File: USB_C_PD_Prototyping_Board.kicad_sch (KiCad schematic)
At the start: 48 parts, among them IC1 TPS259474LRPWR, IC2 BD33FC0FP-E2, J1 USB_C_Receptacle, J2 Power_out, J3 Data_out, J5 Conn_01x04_Pin, J6 Conn_02x02_Counter_Clockwise, J7 Conn_02x02_Counter_Clockwise, Q1 DMP3018SFV-7, Q2 DMP3018SFV-7, SW1 Power_out_switch, U1 HUSB238_xxxDD

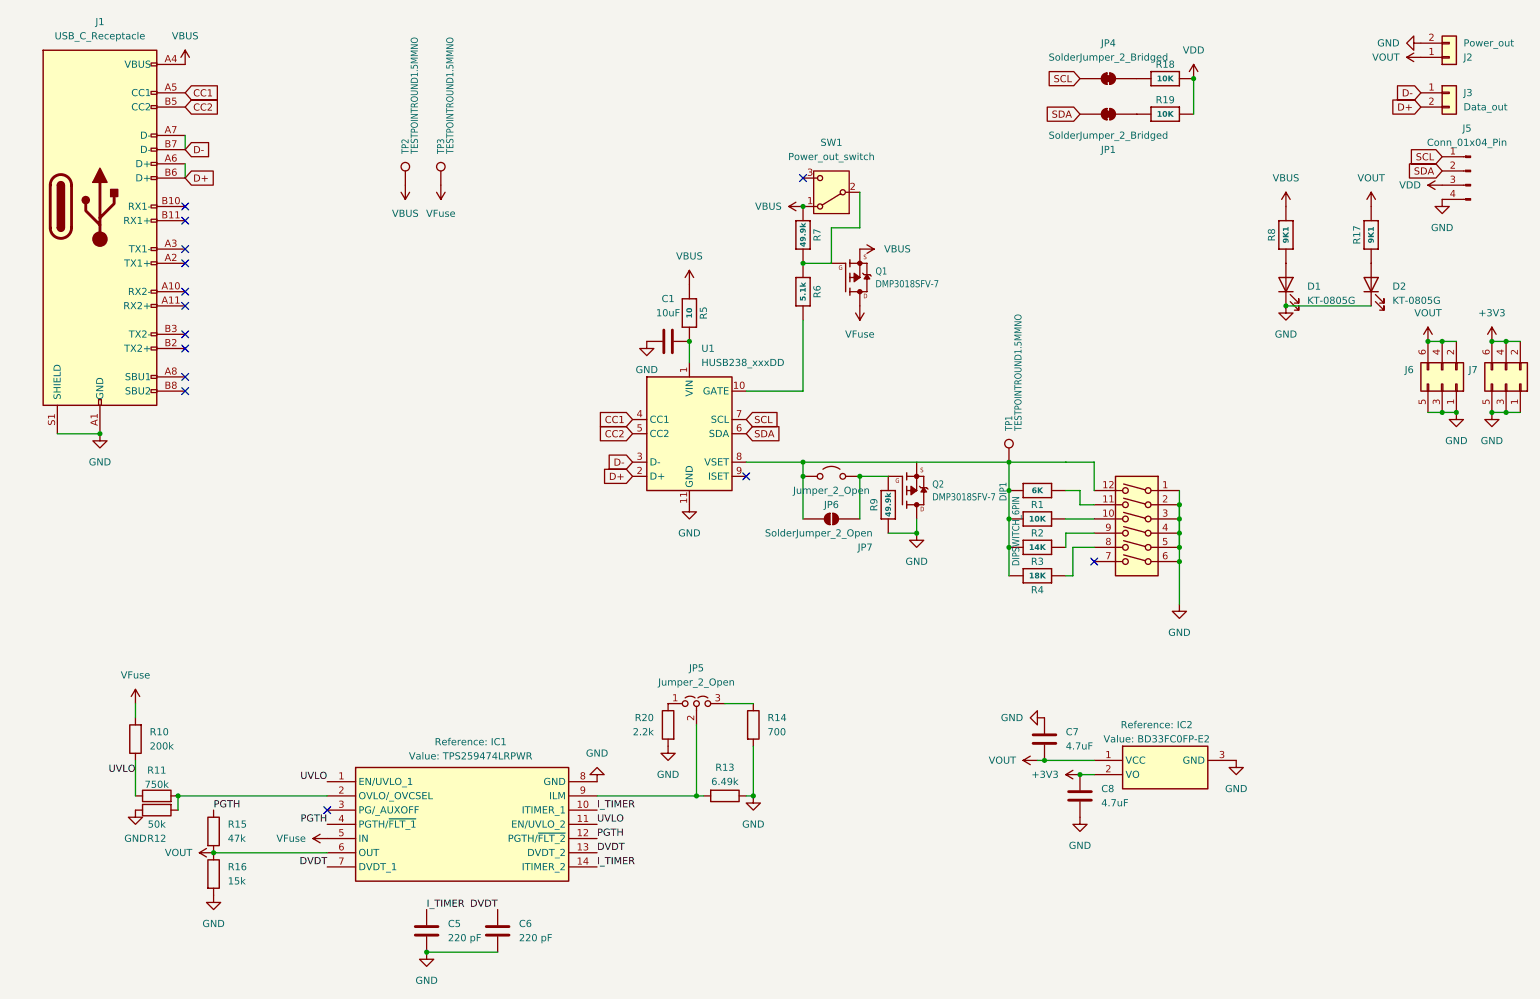
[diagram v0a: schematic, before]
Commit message: Re-worked after initial tests
- Corrected silkscreen labels for output switch
- Corrected jumper logic polarity for voltage select
- Added ISET resistor to set default current request to 3A (instead of 3.25A for open circuit) so that 9, 12V selectable with DIP switches
- Double indicator LED limiting resistor values to reduce brightness
- Changed 3V3 reg to switch mode to solve thermals
- Added cutout to limit covering of breadboard rows
- Made as many resistors as possible THT to use as a soldering task (will spin up an SMD only one as a cheaper out of the box solution too)
- Simplified and thickened primary current path (there wasn't a problem, but it will be more capable now)
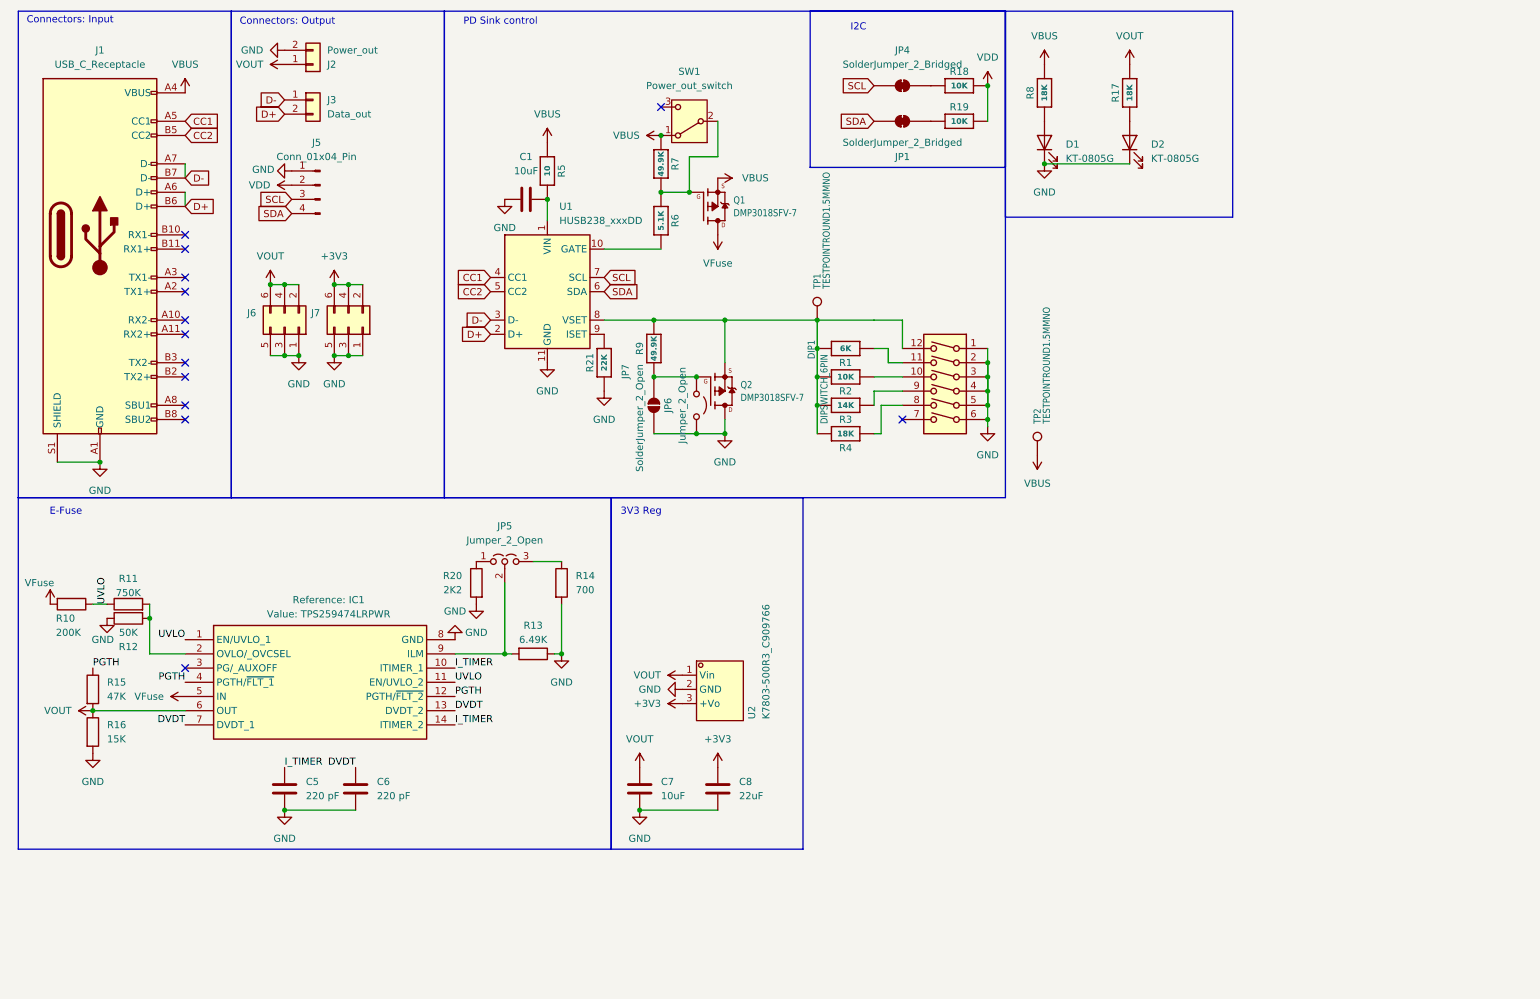
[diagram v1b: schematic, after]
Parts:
- removed IC2: BD33FC0FP-E2, Package_TO_SOT_SMD:TO-252-2, symbol Samacsys:BD33FC0FP-E2
- removed TP3: TESTPOINTROUND1.5MMNO, TestPoint:TestPoint_THTPad_2.0x2.0mm_Drill1.0mm, symbol Connector:TestPoint
- added R21: 22K, Resistor_THT:R_Axial_DIN0207_L6.3mm_D2.5mm_P7.62mm_Horizontal, symbol Adafruit USB Type C PD Switchable-eagle-import:microbuilder_RESISTOR_0402NO
- added U2: K7803-500R3_C909766, EasyEDA:PWRM-TH_K78XX-500R3, symbol EasyEDA:K7803-500R3_C909766
- C7: value 4.7uF -> 10uF
- C8: value 4.7uF -> 22uF
- R1, R14, R2, R3, R4, R5: footprint Resistor_SMD:R_0402_1005Metric_Pad0.72x0.64mm_HandSolder -> Resistor_THT:R_Axial_DIN0207_L6.3mm_D2.5mm_P7.62mm_Horizontal
- R10: value 200k -> 200K; footprint Resistor_SMD:R_0402_1005Metric_Pad0.72x0.64mm_HandSolder -> Resistor_THT:R_Axial_DIN0207_L6.3mm_D2.5mm_P7.62mm_Horizontal
- R11: value 750k -> 750K; footprint Resistor_SMD:R_0402_1005Metric_Pad0.72x0.64mm_HandSolder -> Resistor_THT:R_Axial_DIN0207_L6.3mm_D2.5mm_P7.62mm_Horizontal
- R12: value 50k -> 50K; footprint Resistor_SMD:R_0402_1005Metric_Pad0.72x0.64mm_HandSolder -> Resistor_THT:R_Axial_DIN0207_L6.3mm_D2.5mm_P7.62mm_Horizontal
- R13: value 6.49k -> 6.49K
- R15: value 47k -> 47K; footprint Resistor_SMD:R_0402_1005Metric_Pad0.72x0.64mm_HandSolder -> Resistor_THT:R_Axial_DIN0207_L6.3mm_D2.5mm_P7.62mm_Horizontal
- R16: value 15k -> 15K; footprint Resistor_SMD:R_0402_1005Metric_Pad0.72x0.64mm_HandSolder -> Resistor_THT:R_Axial_DIN0207_L6.3mm_D2.5mm_P7.62mm_Horizontal
- R17, R8: value 9K1 -> 18K; footprint Resistor_SMD:R_0402_1005Metric_Pad0.72x0.64mm_HandSolder -> Resistor_THT:R_Axial_DIN0207_L6.3mm_D2.5mm_P7.62mm_Horizontal
- R20: value 2.2k -> 2K2; footprint Resistor_SMD:R_0402_1005Metric_Pad0.72x0.64mm_HandSolder -> Resistor_THT:R_Axial_DIN0207_L6.3mm_D2.5mm_P7.62mm_Horizontal
- R6: value 5.1k -> 5.1K
- R7, R9: value 49.9k -> 49.9K; footprint Resistor_SMD:R_0402_1005Metric_Pad0.72x0.64mm_HandSolder -> Resistor_THT:R_Axial_DIN0207_L6.3mm_D2.5mm_P7.62mm_Horizontal
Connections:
- net +3V3: now also U2.3 (+Vo)
- net GND: now also C7.1, J5.1 (Pin_1), JP6.2 (B), JP7.2 (B), R21.1, U2.2 (GND); no longer C7.2, J5.4 (Pin_4), R9.1
- net SCL: now also J5.3 (Pin_3); no longer J5.1 (Pin_1)
- net SDA: now also J5.4 (Pin_4); no longer J5.2 (Pin_2)
- net VDD: now also J5.2 (Pin_2); no longer J5.3 (Pin_3)
- net VOUT: now also C7.2, U2.1 (Vin); no longer C7.1
- net at DIP1.12, R1.2, R2.2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: now also Q2.1 (S), Q2.2 (S), Q2.3 (S), R9.2; no longer JP6.2 (B), JP7.2 (B)
- net at JP6.1 (A), JP7.1 (A), Q2.4 (G): now also R9.1; no longer R9.2
- net at U1.9 (ISET): now also R21.2
- no-connect marks 14 -> 13
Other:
- note added: "3V3 Reg"
- note added: "Connectors: Input"
- note added: "Connectors: Output"
- note added: "E-Fuse"
- note added: "I2C"
- note added: "PD Sink control"
- moved on the sheet: C1, C5, C6, D1, D2, DIP1, J1, J2, J3, J5, J6, J7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
